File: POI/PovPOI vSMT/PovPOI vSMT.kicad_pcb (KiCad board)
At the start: 2 copper layers, 21 x 52.2 mm, 22 parts, among them J2 Conn_01x08, J3 Conn_01x04, J4 Conn_01x08, J5 Conn_01x04, Q1 Q_NMOS_GDSD, SW1 SW_SPST, SW2 SW_SPST, U2 ADXL345BCCZ-RL7

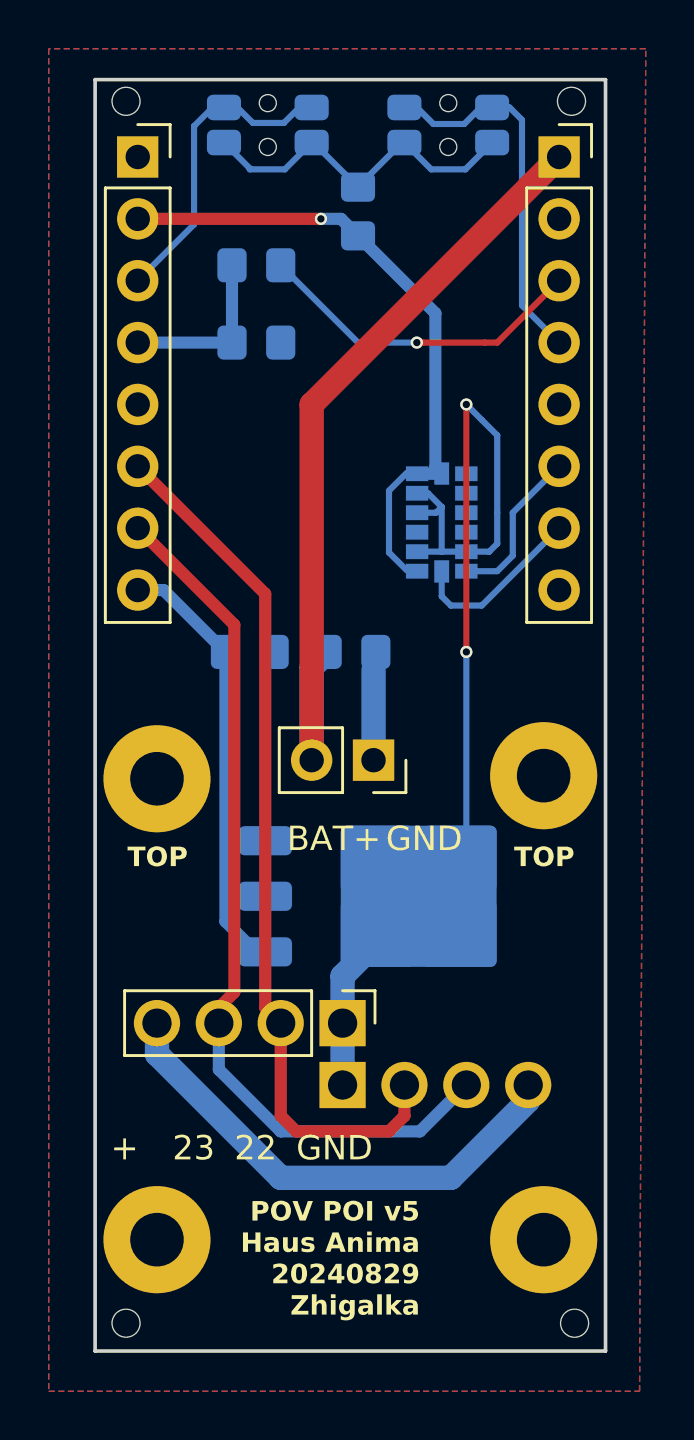
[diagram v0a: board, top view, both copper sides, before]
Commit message: Reloaded PovPOI vSMT from worklaptop
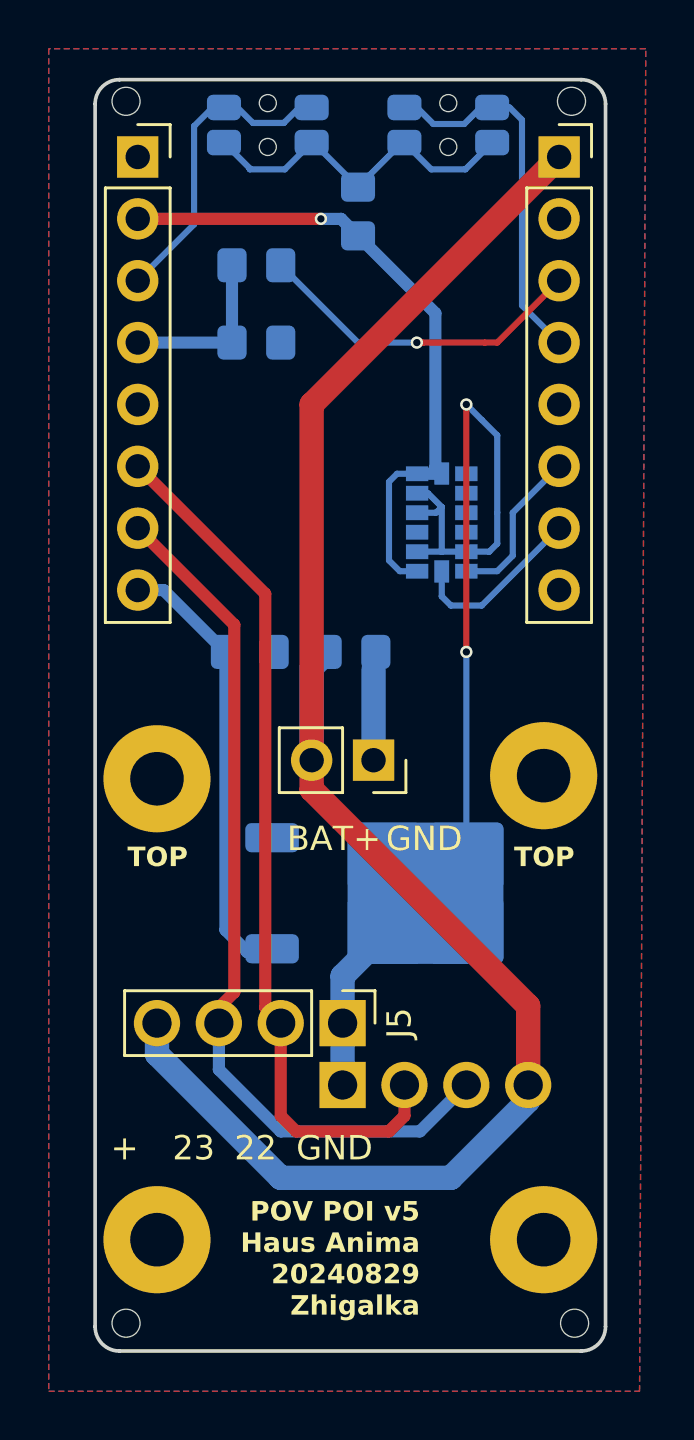
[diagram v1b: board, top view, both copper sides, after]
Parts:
- removed Q1: Q_NMOS_GDSD, Package_TO_SOT_SMD:TO-252-3_TabPin4
- added Q2: Q_NMOS_GDS, Package_TO_SOT_SMD:TO-252-2, B.Cu at (39.0, 59.4)
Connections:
- J3 pad 4: /V_LED -> /BAT+_TERMINAL
- J5 pad 4: /V_LED -> /BAT+_TERMINAL
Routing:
- net /BAT+_TERMINAL: track 33.7 -> 71.3 mm
- net /V_LED: track 20.6 -> 0.00 mm
- net /3V3: track 26.3 -> 27.6 mm
- net /IO7: track 17.9 -> 18.8 mm
- net Net-(SW1-A): track 14.9 -> 14.4 mm
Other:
- outline, holes or cut-outs redrawn
